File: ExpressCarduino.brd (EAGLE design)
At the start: 14.9 x 27.9 mm, 1 part

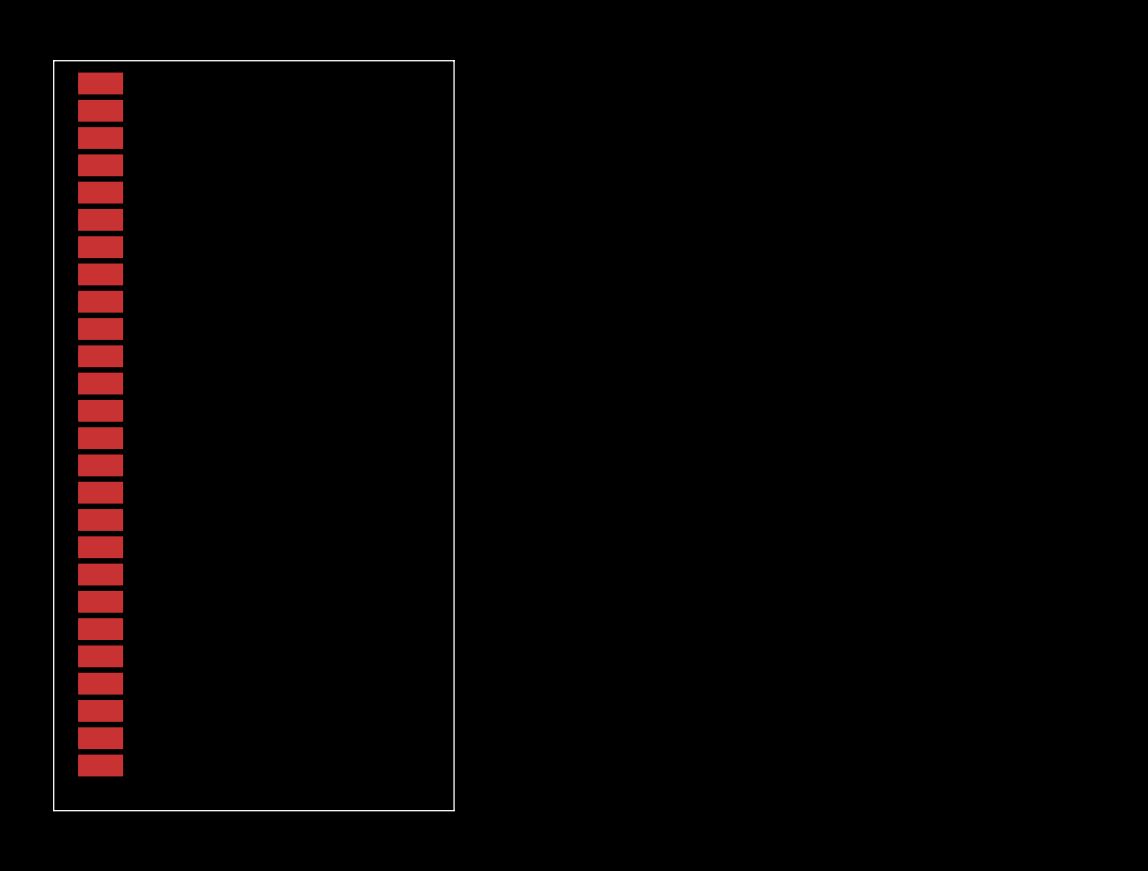
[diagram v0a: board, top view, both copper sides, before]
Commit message: Added vreg circuit for 3.3v -> 9v and images
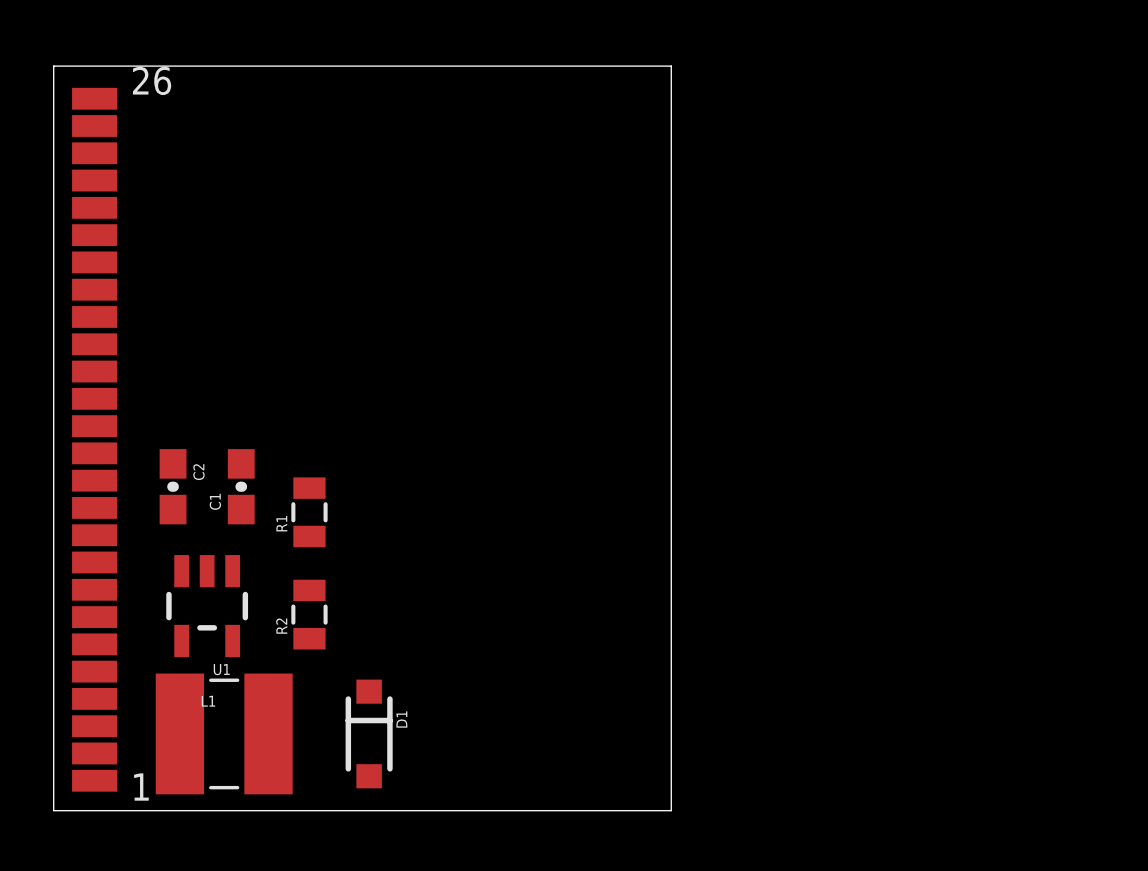
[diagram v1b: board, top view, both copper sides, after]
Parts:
- added C1, C2: 1.0uF, SparkFun-Capacitors:0603-CAP
- added D1: 1N5819, HokieGeek:SOD-123
- added L1: 56uH, SparkFun-Passives:SDR0403
- added R1: 41.2K, SparkFun-Resistors:0805
- added R2: 6.5K, SparkFun-Resistors:0805
- added U1: 74LVC1G08, HokieGeek:SOT23-5
- moved U$1 5.09 mm to (1.59, 14.0)
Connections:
- net 3.3V_B renamed 3.3V
- removed net 1.5V_A: U$1.P$9
- removed net 1.5V_B: U$1.P$10
- removed net 3.3V_A: U$1.P$14
- removed net GND_A: U$1.P$1
- removed net GND_B: U$1.P$20
- removed net GND_C: U$1.P$23
- removed net GND_D: U$1.P$26
- new net 1.5V: U$1.P$10, U$1.P$9
- new net 9V: C1.1, D1.C, R1.2
- new net GND: C1.2, C2.2, R2.1, U$1.P$1, U$1.P$20, U$1.P$23, U$1.P$26, U$1.P$4, U1.2
- new net N$1: R1.1, R2.2, U1.3
- new net N$2: C2.1, L1.P$1, U$1.P$14, U$1.P$5, U1.4, U1.5
- new net N$3: D1.A, L1.P$2, U1.1
- new net N$4: U$1.P$2
- new net N$5: U$1.P$3
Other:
- board size 14.9 x 27.9 mm -> 23 x 27.7 mm
- board text added: "Arduino Metro"

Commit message: Added the Mini USB part
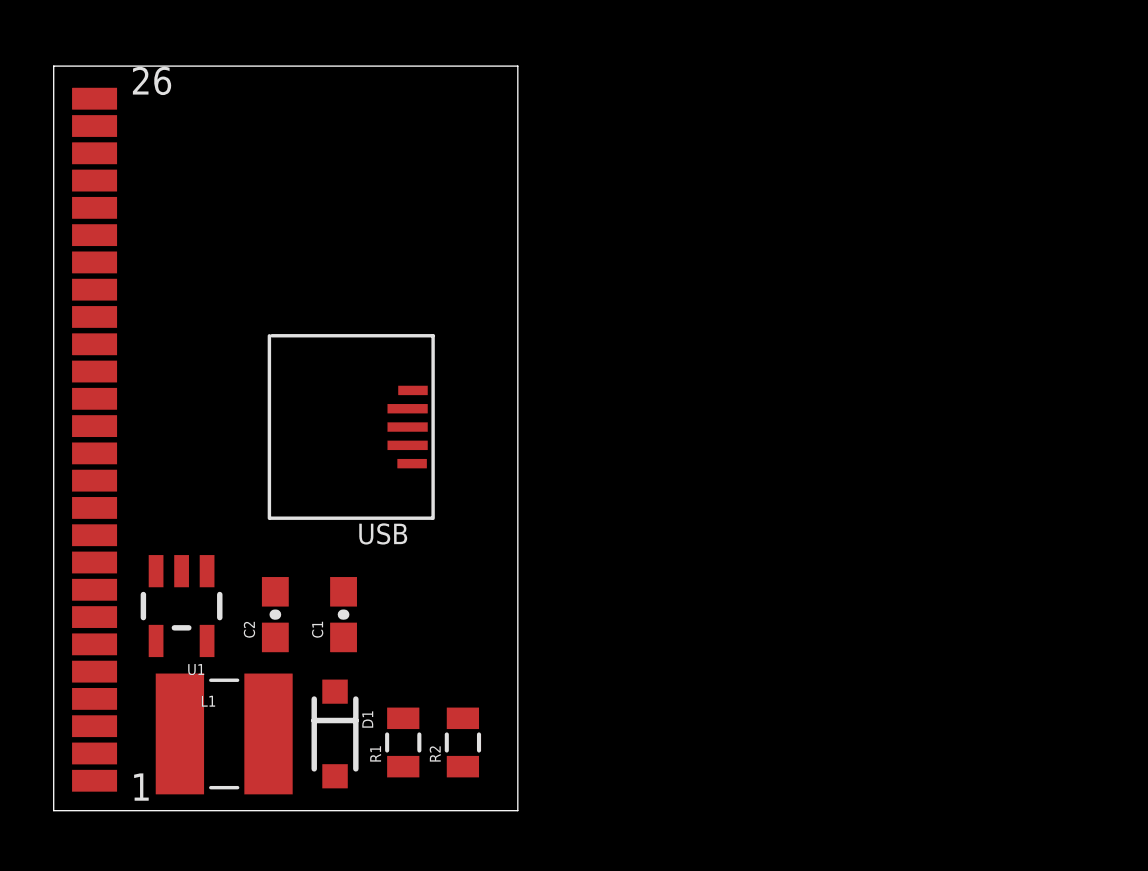
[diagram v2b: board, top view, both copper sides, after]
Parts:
- added USB: (no value), HokieGeek:MICRO-B-RA-SMT
- moved R1 9.26 mm to (13.0, 2.54)
- moved R2 7.44 mm to (15.2, 2.54)
- moved C2 6.10 mm to (8.26, 7.30), turned to 90 degrees
- moved C1 6.10 mm to (10.8, 7.30)
- moved D1 1.27 mm to (10.5, 2.86)
- moved U1 0.95 mm to (4.76, 7.62)
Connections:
- removed net N$4: U$1.P$2
- removed net N$5: U$1.P$3
- new net USBD+: U$1.P$3, USB.3
- new net USBD-: U$1.P$2, USB.2
- net 9V: now also USB.1
- net GND: now also USB.5
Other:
- board size 23 x 27.7 mm -> 17.3 x 27.7 mm
- board text added: "Adafruit Metro Mini 328"
- board text removed: "Arduino Metro"
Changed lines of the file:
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@@
 <board>
 <plain>
-<wire x1="0" y1="0" x2="23" y2="0" width="0" layer="20"/>
-<wire x1="23" y1="0" x2="23" y2="27.73" width="0" layer="20"/>
-<wire x1="23" y1="27.73" x2="0" y2="27.73" width="0" layer="20"/>
+<wire x1="0" y1="0" x2="17.285" y2="0" width="0" layer="20"/>
+<wire x1="17.285" y1="0" x2="17.285" y2="27.73" width="0" layer="20"/>
+<wire x1="17.285" y1="27.73" x2="0" y2="27.73" width="0" layer="20"/>
 <wire x1="0" y1="27.73" x2="0" y2="0" width="0" layer="20"/>
-<rectangle x1="19.05" y1="5.08" x2="63.05" y2="23.08" layer="51"/>
-<text x="33.02" y="24.13" size="1.778" layer="51">Arduino Metro</text>
+<rectangle x1="19.05" y1="5.08" x2="63.05" y2="23.08" layer="41"/>
+<text x="28.2575" y="23.1775" size="1.778" layer="51">Adafruit Metro Mini 328</text>
 <dimension x1="65.2275" y1="-0.3175" x2="65.2275" y2="27.4125" x3="68.5364875" y3="13.5475" textsize="1.778" layer="51"/>
-<dimension x1="0" y1="27.73" x2="65.0875" y2="27.6225" x3="32.5484875" y3="30.546021875" textsize="1.778" layer="51"/>
+<dimension x1="0" y1="27.73" x2="65.0875" y2="27.73" x3="32.54375" y3="30.546021875" textsize="1.778" layer="51"/>
 </plain>
 <attributes>
@@
 <param name="RoutingGrid" value="50mil"/>
 <param name="AutoGrid" value="1"/>
-<param name="Efforts" value="0"/>
+<param name="Efforts" value="2"/>
 <param name="TopRouterVariant" value="1"/>
 <param name="tpViaShape" value="round"/>
@@
 <elements>
 <element name="U$1" library="HokieGeek" package="EXPRESSCARD34" value="EXPRESSCARD34" x="1.5875" y="13.97"/>
-<element name="R1" library="SparkFun-Resistors" package="0805" value="41.2K" x="9.525" y="11.1125" rot="R90">
-<attribute name="PROD_ID" value="RES-09883" x="9.525" y="11.1125" size="1.778" layer="27" rot="R90" display="off"/>
-</element>
-<element name="R2" library="SparkFun-Resistors" package="0805" value="6.5K" x="9.525" y="7.3025" rot="R90">
-<attribute name="PROD_ID" value="RES-09883" x="9.525" y="7.3025" size="1.778" layer="27" rot="R90" display="off"/>
-</element>
-<element name="U1" library="HokieGeek" package="SOT23-5" value="74LVC1G08" x="5.715" y="7.62" rot="R180">
-<attribute name="PROD_ID" value="10841" x="5.715" y="7.62" size="1.778" layer="27" rot="R180" display="off"/>
-</element>
-<element name="C1" library="SparkFun-Capacitors" package="0603-CAP" value="1.0uF" x="6.985" y="12.065" rot="R90">
-<attribute name="PROD_ID" value="CAP-00868" x="6.985" y="12.065" size="1.778" layer="27" rot="R90" display="off"/>
-</element>
-<element name="C2" library="SparkFun-Capacitors" package="0603-CAP" value="1.0uF" x="4.445" y="12.065" rot="R270">
-<attribute name="PROD_ID" value="CAP-00868" x="4.445" y="12.065" size="1.778" layer="27" rot="R270" display="off"/>
+<element name="R1" library="SparkFun-Resistors" package="0805" value="41.2K" x="13.0175" y="2.54" rot="R90">
+<attribute name="PROD_ID" value="RES-09883" x="13.0175" y="2.54" size="1.778" layer="27" rot="R90" display="off"/>
+</element>
+<element name="R2" library="SparkFun-Resistors" package="0805" value="6.5K" x="15.24" y="2.54" rot="R90">
+<attribute name="PROD_ID" value="RES-09883" x="15.24" y="2.54" size="1.778" layer="27" rot="R90" display="off"/>
+</element>
+<element name="U1" library="HokieGeek" package="SOT23-5" value="74LVC1G08" x="4.7625" y="7.62" rot="R180">
+<attribute name="PROD_ID" value="10841" x="4.7625" y="7.62" size="1.778" layer="27" rot="R180" display="off"/>
+</element>
+<element name="C1" library="SparkFun-Capacitors" package="0603-CAP" value="1.0uF" x="10.795" y="7.3025" rot="R90">
+<attribute name="PROD_ID" value="CAP-00868" x="10.795" y="7.3025" size="1.778" layer="27" rot="R90" display="off"/>
+</element>
+<element name="C2" library="SparkFun-Capacitors" package="0603-CAP" value="1.0uF" x="8.255" y="7.3025" rot="R90">
+<attribute name="PROD_ID" value="CAP-00868" x="8.255" y="7.3025" size="1.778" layer="27" rot="R90" display="off"/>
 </element>
 <element name="L1" library="SparkFun-Passives" package="SDR0403" value="56uH" x="6.35" y="2.8575">
@@
 <attribute name="DIST" value="DIGIKEY" x="6.35" y="2.8575" size="1.778" layer="27" display="off"/>
 </element>
-<element name="D1" library="HokieGeek" package="SOD-123" value="1N5819" x="11.7475" y="2.8575" rot="R270"/>
+<element name="D1" library="HokieGeek" package="SOD-123" value="1N5819" x="10.4775" y="2.8575" rot="R270"/>
+<element name="USB" library="HokieGeek" package="MICRO-B-RA-SMT" value="" x="11.43" y="14.2875" rot="R90"/>
 </elements>
 <signals>
@@
 <contactref element="L1" pad="P$1"/>
 <contactref element="U1" pad="4"/>
-<wire x1="1.5216375" y1="14.322471875" x2="4.445" y2="12.915" width="0" layer="19" extent="1-1"/>
-<wire x1="4.765" y1="6.3199" x2="4.445" y2="12.915" width="0" layer="19" extent="1-1"/>
-<wire x1="6.665" y1="6.3199" x2="4.765" y2="6.3199" width="0" layer="19" extent="1-1"/>
-<wire x1="1.5216375" y1="5.178471875" x2="4.765" y2="6.3199" width="0" layer="19" extent="1-1"/>
-<wire x1="4.7" y1="2.8575" x2="4.765" y2="6.3199" width="0" layer="19" extent="1-1"/>
-</signal>
-<signal name="N$4">
+<wire x1="3.8125" y1="6.3199" x2="1.5216375" y2="14.322471875" width="0" layer="19" extent="1-1"/>
+<wire x1="5.7125" y1="6.3199" x2="3.8125" y2="6.3199" width="0" layer="19" extent="1-1"/>
+<wire x1="8.255" y1="6.4525" x2="5.7125" y2="6.3199" width="0" layer="19" extent="1-1"/>
+<wire x1="1.5216375" y1="5.178471875" x2="3.8125" y2="6.3199" width="0" layer="19" extent="1-1"/>
+<wire x1="4.7" y1="2.8575" x2="3.8125" y2="6.3199" width="0" layer="19" extent="1-1"/>
+</signal>
+<signal name="USBD-">
 <contactref element="U$1" pad="P$2"/>
-</signal>
-<signal name="N$5">
+<contactref element="USB" pad="2"/>
+<wire x1="1.5216375" y1="2.130471875" x2="13.18" y2="14.96925" width="0" layer="19" extent="1-1"/>
+</signal>
+<signal name="USBD+">
 <contactref element="U$1" pad="P$3"/>
+<contactref element="USB" pad="3"/>
+<wire x1="1.5216375" y1="3.146471875" x2="13.18" y2="14.2875" width="0" layer="19" extent="1-1"/>
 </signal>
 <signal name="GND">
@@
 <contactref element="C1" pad="2"/>
 <contactref element="C2" pad="2"/>
+<contactref element="USB" pad="5"/>
 <wire x1="1.5216375" y1="23.466471875" x2="1.5216375" y2="26.514471875" width="0" layer="19" extent="1-1"/>
 <wire x1="1.5216375" y1="20.418471875" x2="1.5216375" y2="23.466471875" width="0" layer="19" extent="1-1"/>
-<wire x1="6.985" y1="12.915" x2="1.5216375" y2="20.418471875" width="0" layer="19" extent="1-1"/>
-<wire x1="4.445" y1="11.215" x2="6.985" y2="12.915" width="0" layer="19" extent="1-1"/>
-<wire x1="5.715" y1="8.9201" x2="4.445" y2="11.215" width="0" layer="19" extent="1-1"/>
-<wire x1="9.525" y1="6.4025" x2="5.715" y2="8.9201" width="0" layer="19" extent="1-1"/>
-<wire x1="1.5216375" y1="4.162471875" x2="5.715" y2="8.9201" width="0" layer="19" extent="1-1"/>
+<wire x1="4.7625" y1="8.9201" x2="1.5216375" y2="20.418471875" width="0" layer="19" extent="1-1"/>
+<wire x1="8.255" y1="8.1525" x2="4.7625" y2="8.9201" width="0" layer="19" extent="1-1"/>
+<wire x1="10.795" y1="8.1525" x2="8.255" y2="8.1525" width="0" layer="19" extent="1-1"/>
+<wire x1="13.34825" y1="12.924" x2="10.795" y2="8.1525" width="0" layer="19" extent="1-1"/>
+<wire x1="1.5216375" y1="4.162471875" x2="4.7625" y2="8.9201" width="0" layer="19" extent="1-1"/>
 <wire x1="1.5216375" y1="1.114471875" x2="1.5216375" y2="4.162471875" width="0" layer="19" extent="1-1"/>
+<wire x1="15.24" y1="1.64" x2="10.795" y2="8.1525" width="0" layer="19" extent="1-1"/>
 </signal>
 <signal name="1.5V">
@@
 <contactref element="R2" pad="2"/>
 <contactref element="R1" pad="1"/>
-<wire x1="9.525" y1="8.2025" x2="9.525" y2="10.2125" width="0" layer="19" extent="1-1"/>
-<wire x1="4.765" y1="8.9201" x2="9.525" y2="8.2025" width="0" layer="19" extent="1-1"/>
+<wire x1="13.0175" y1="1.64" x2="15.24" y2="3.44" width="0" layer="19" extent="1-1"/>
+<wire x1="3.8125" y1="8.9201" x2="13.0175" y2="1.64" width="0" layer="19" extent="1-1"/>
 </signal>
 <signal name="9V">
@@
 <contactref element="C1" pad="1"/>
 <contactref element="D1" pad="C"/>
-<wire x1="6.985" y1="11.215" x2="9.525" y2="12.0125" width="0" layer="19" extent="1-1"/>
-<wire x1="11.7475" y1="4.4325" x2="6.985" y2="11.215" width="0" layer="19" extent="1-1"/>
+<contactref element="USB" pad="1"/>
+<wire x1="10.795" y1="6.4525" x2="13.38" y2="15.651" width="0" layer="19" extent="1-1"/>
+<wire x1="10.4775" y1="4.4325" x2="10.795" y2="6.4525" width="0" layer="19" extent="1-1"/>
+<wire x1="13.0175" y1="3.44" x2="10.4775" y2="4.4325" width="0" layer="19" extent="1-1"/>
 </signal>
 <signal name="N$3">
@@
 <contactref element="L1" pad="P$2"/>
 <contactref element="U1" pad="1"/>
-<wire x1="8" y1="2.8575" x2="6.665" y2="8.9201" width="0" layer="19" extent="1-1"/>
-<wire x1="11.7475" y1="1.2825" x2="8" y2="2.8575" width="0" layer="19" extent="1-1"/>
+<wire x1="8" y1="2.8575" x2="5.7125" y2="8.9201" width="0" layer="19" extent="1-1"/>
+<wire x1="10.4775" y1="1.2825" x2="8" y2="2.8575" width="0" layer="19" extent="1-1"/>
 </signal>
 </signals>

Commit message: Added an IO expander and more ADC lines. Not sure why, tbh
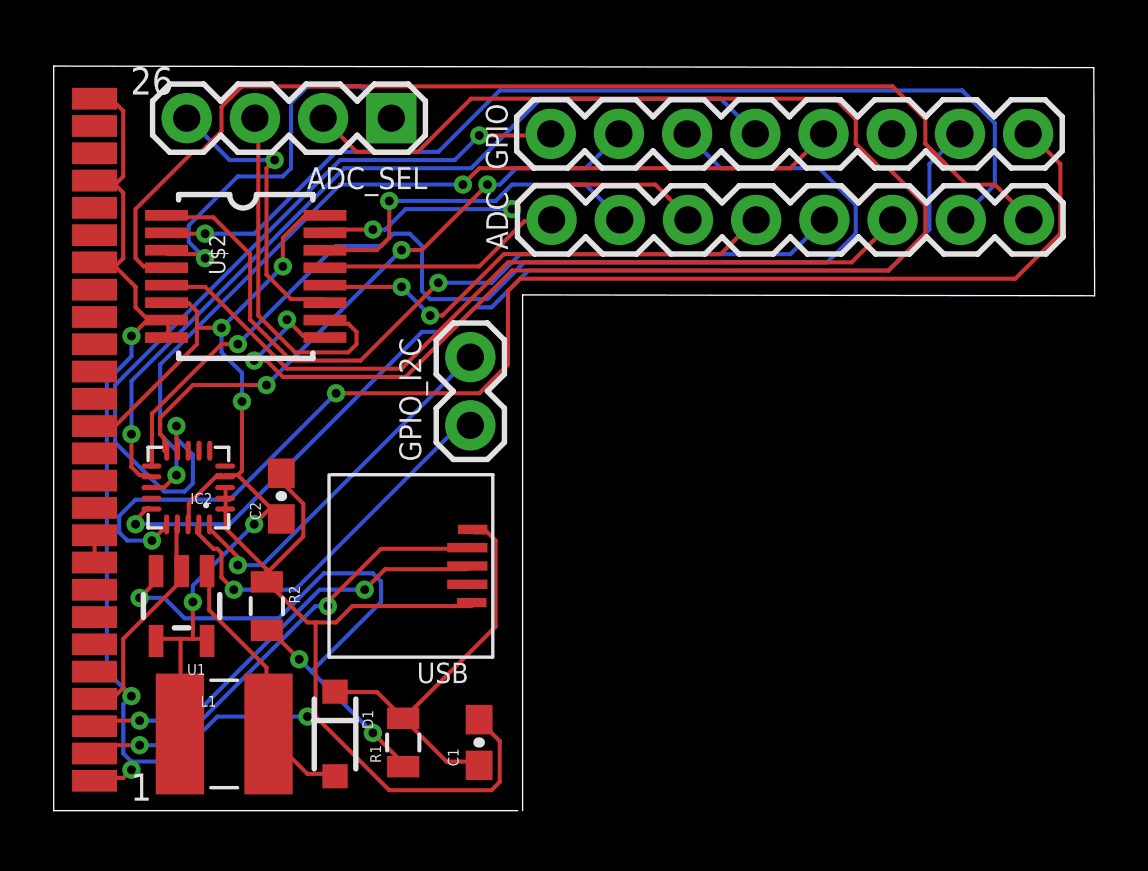
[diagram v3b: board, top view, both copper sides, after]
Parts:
- added ADC, GPIO: (no value), SparkFun-Connectors:1X08_ROUND
- added ADC_SEL: (no value), SparkFun-Connectors:1X04
- added GPIO_I2C: (no value), SparkFun-Connectors:1X02
- added IC2: MCP23008, HokieGeek:QFN-20-0.4MM-V2
- added U$2: SN74LV4051A, HokieGeek:TSSOP16
- U1: value 74LVC1G08 -> AP3012
- moved R2 8.90 mm to (7.94, 7.62), turned to 270 degrees
- moved C1 6.94 mm to (15.8, 2.54)
- moved USB 5.63 mm to (13.7, 9.11)
- moved C2 4.42 mm to (8.48, 11.7)
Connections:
- net 3.3V renamed 3.3V_B
- new net 3.3V_A: C2.1, IC2.18, IC2.4, L1.P$1, U$1.P$14, U$2.16, U$2.6, U1.4, U1.5
- new net N$10: GPIO.8, IC2.16
- new net N$11: GPIO_I2C.1, IC2.19
- new net N$12: GPIO_I2C.2, IC2.20
- new net N$13: ADC_SEL.1, U$2.3
- new net N$19: ADC.1, U$2.13
- new net N$20: ADC.2, U$2.14
- new net N$21: ADC.3, U$2.15
- new net N$22: ADC.4, U$2.12
- new net N$23: ADC.5, U$2.1
- new net N$24: ADC.6, U$2.5
- new net N$25: ADC.7, U$2.2
- new net N$26: ADC.8, U$2.4
- new net N$29: ADC_SEL.2, U$2.9
- new net N$30: ADC_SEL.3, U$2.10
- new net N$31: ADC_SEL.4, U$2.11
- new net N$4: GPIO.2, IC2.10
- new net N$5: GPIO.3, IC2.11
- new net N$6: GPIO.4, IC2.12
- new net N$7: GPIO.5, IC2.13
- new net N$8: GPIO.6, IC2.14
- new net N$9: GPIO.7, IC2.15
- net GND: now also IC2.1, IC2.17, IC2.2, IC2.3, U$2.7, U$2.8
- net N$2: now also GPIO.1, IC2.9; no longer C2.1, L1.P$1, U$1.P$14, U$1.P$5, U1.4, U1.5
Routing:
- net GND: track 0.00 -> 83.5 mm, vias 0 -> 4
- net N$29: track 0.00 -> 58.2 mm, vias 0 -> 2
- net N$10: track 0.00 -> 48.0 mm, vias 0 -> 2
- net N$5: track 0.00 -> 42.5 mm, vias 0 -> 1
- net N$26: track 0.00 -> 41.4 mm
- net N$9: track 0.00 -> 39.1 mm, vias 0 -> 1
- net 3.3V_A: track 0.00 -> 38.1 mm, vias 0 -> 5
- net N$25: track 0.00 -> 37.7 mm, vias 0 -> 1
- net N$7: track 0.00 -> 33.8 mm, vias 0 -> 2
- net N$6: track 0.00 -> 32.2 mm, vias 0 -> 1
- net N$24: track 0.00 -> 30.7 mm
- net N$23: track 0.00 -> 30.3 mm, vias 0 -> 1
- net N$2: track 0.00 -> 29.4 mm, vias 0 -> 2
- net N$1: track 0.00 -> 23.2 mm, vias 0 -> 3
- net N$4: track 0.00 -> 22.9 mm, vias 0 -> 3
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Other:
- board size 17.3 x 27.7 mm -> 38.8 x 27.7 mm
